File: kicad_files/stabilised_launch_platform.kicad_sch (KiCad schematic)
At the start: 2 parts

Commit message: Added further components to schematic
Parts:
- added C? (x3): 10u, symbol Device:C
- added C? (x4): 0.1u, symbol Device:C
- added C?: 1u, symbol Device:C
- added J? (x2): Conn_01x03_Male, symbol Connector:Conn_01x03_Male
- added J?: Conn_01x04_Male, symbol Connector:Conn_01x04_Male
- added R? (x2): R, symbol Device:R
- added RV? (x3): R_Potentiometer, symbol Device:R_Potentiometer
- added SW?: SW_Push, symbol Switch:SW_Push
- added U?: AP7370-33Y, Package_TO_SOT_SMD:SOT-89-3, symbol Regulator_Linear:AP7384-33Y
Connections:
- net SCL: now reaches U?.10 (PA4)
- net SCL: now also R?.2
- net POT1: now reaches U?.13 (PA7)
- net POT1: now also RV?.2
- net GND: now reaches U?.15 (VSS)
- net GND: now also U?.3 (GND), C?.2, C?.2, C?.2, C?.2, C?.2, C?.2, C?.2, C?.2, J?.3 (Pin_3), J?.3 (Pin_3), J?.4 (Pin_4), RV?.3, RV?.3, RV?.3, SW?.1, U?.2 (GND)
- net +3.3V: now reaches U?.16 (VDD)
- net +3.3V: now also U?.1 (V+), U?.5 (VDDA), C?.1, C?.1, C?.1, C?.1, C?.1, C?.1, R?.1, R?.1, RV?.1, RV?.1, RV?.1, U?.1 (VO)
- net SDA: now reaches U?.18 (PA10)
- net SDA: now also R?.2
- net SWDIO: now reaches U?.19 (PA13)
- net SWDIO: now also J?.2 (Pin_2)
- net SWCLK: now reaches U?.20 (PA14)
- net SWCLK: now also J?.3 (Pin_3)
- net at U?.4 (NRST): now also C?.1, SW?.2
- net HSE_OSC: now reaches U?.6 (PA0)
- net HSE_OSC: now also U?.2 (CLOCK)
- new net +5V: C?.1, J?.1 (Pin_1), J?.2 (Pin_2), J?.2 (Pin_2), U?.3 (VI)
- new net POT2: RV?.2
- new net POT3: RV?.2
- new net SERVO1_SIG: J?.1 (Pin_1)
- new net SERVO2_SIG: J?.1 (Pin_1)
- no-connect marks 0 -> 2
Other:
- note added: "8MHz External Clock"
- note added: "MCU Decoupling Capacitors"
- note added: "PID Gain Potentiometers"
- note added: "ST-LINK Connector"
- note added: "Servo Motor Connectors"
- note added: "Voltage Regulator"
- moved on the sheet: U?

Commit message: component values
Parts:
- R1, R2: renamed from R?; value R -> 2.2k
- gave numbers to parts that had none: 18

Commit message: added more components
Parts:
- removed J3: Conn_01x04_Male, symbol Connector:Conn_01x04_Male
- added C10, C13: 47p, symbol Device:C
- added C11: 10n, symbol Device:C
- added C12, C9: 0.1u, symbol Device:C
- added C14: 4.7u, symbol Device:C_Polarized
- added FB1: FerriteBead, symbol Device:FerriteBead
- added J3: Conn_01x06_Male, symbol Connector:Conn_01x06_Male
- added J4: USB_C_Receptacle_USB2.0, symbol Connector:USB_C_Receptacle_USB2.0
- added JP1: SolderJumper, symbol Jumper:SolderJumper_2_Open
- added R3, R4: 5.1k, symbol Device:R
- added R5, R6: 2.2k, symbol Device:R
- added U4: FT201XS, Package_SO:SSOP-16_3.9x4.9mm_P0.635mm, symbol Interface_USB:FT201XS
- R1, R2: value 2.2k -> 27R
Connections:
- net +3.3V: now also U3.1 (PB9), R5.1, R6.1; no longer R1.1, R2.1
- net +5V: now also C14.1, C9.1, FB1.2, J3.1 (Pin_1), JP1.1 (A)
- net GND: now also C10.2, C11.2, C12.2, C13.2, C14.2, C9.2, J3.6 (Pin_6), J4.A1 (GND), J4.A12 (GND), J4.B1 (GND), J4.B12 (GND), J4.S1 (SHIELD), R3.2, R4.2, U4.13 (GND), U4.5 (GND)
- net POT1: now also U3.11 (PA5); no longer U3.13 (PA7)
- net POT2: now also U3.12 (PA6)
- net POT3: now also U3.13 (PA7)
- net SCL: now also U3.17 (PA9), R5.2, U4.2 (SCL); no longer R1.2, U3.10 (PA4)
- net SDA: now also R6.2, U4.4 (SDA); no longer R2.2
- net SERVO1_SIG: now also U3.7 (PA1)
- net SERVO2_SIG: now also U3.10 (PA4)
- net SWCLK: now also J3.3 (Pin_3)
- net SWDIO: now also J3.2 (Pin_2)
- net MCU_TX: now reaches U3.8 (PA2)
- net MCU_TX: now also J3.4 (Pin_4)
- net MCU_RX: now reaches U3.9 (PA3)
- net MCU_RX: now also J3.5 (Pin_5)
- new net: J4.B5 (CC2), R4.1
- new net: R2.2, U4.8 (USBDP)
- new net: JP1.2 (B), U4.12 (VCC)
- new net: R1.2, U4.9 (USBDM)
- new net: J4.A5 (CC1), R3.1
- new net: C11.1, FB1.1, J4.A4 (VBUS), J4.A9 (VBUS), J4.B4 (VBUS), J4.B9 (VBUS)
- new net FTDI_3V3: C12.1, U4.10 (3V3OUT), U4.11 (~{RESET}), U4.3 (VCCIO)
- new net USBDM: C13.1, J4.A7 (D-), J4.B7 (D-), R1.1
- new net USBDP: C10.1, J4.A6 (D+), J4.B6 (D+), R2.1
- no-connect marks 2 -> 11
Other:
- note added: "I2C Pull-up"
- note added: "Microcontroller"
- note added: "USB C Receptacle"
- note added: "USB to I2C"
- moved on the sheet: RV1, RV2, RV3

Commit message: Schematic finished
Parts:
- added Q1, Q2: AO3400A, Package_TO_SOT_SMD:SOT-23, symbol Transistor_FET:AO3400A
- added R7, R8: 4.7k, Resistor_SMD:R_0805_2012Metric_Pad1.20x1.40mm_HandSolder, symbol Device:R
- added U5: LIS3DH, Package_LGA:LGA-16_3x3mm_P0.5mm_LayoutBorder3x5y, symbol Sensor_Motion:LIS3DH
- C1, C10, C11, C12, C13, C14, C2, C3, C4, C5, C6, C7, C8, C9: footprint (none) -> Capacitor_SMD:C_0805_2012Metric_Pad1.18x1.45mm_HandSolder
- J1, J2: footprint (none) -> Connector_PinHeader_1.00mm:PinHeader_1x03_P1.00mm_Vertical
- J3: footprint (none) -> Connector_PinHeader_1.00mm:PinHeader_1x06_P1.00mm_Vertical
- J4: footprint (none) -> Connector_USB:USB_C_Receptacle_GCT_USB4085
- R1, R2, R3, R4, R5, R6: footprint (none) -> Resistor_SMD:R_0805_2012Metric_Pad1.20x1.40mm_HandSolder
- RV1, RV2, RV3: footprint (none) -> Potentiometer_THT:Potentiometer_Bourns_PTA4543_Single_Slide
- SW1: footprint (none) -> Button_Switch_SMD:SW_SPST_PTS645
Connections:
- net +3.3V: now also U5.14 (VDD)
- net +5V: now also R7.1, R8.1
- net GND: now also Q1.2 (S), Q2.2 (S), U5.10 (GND), U5.12 (GND), U5.5 (GND)
- net SCL: now also U5.4 (SCL/SPC)
- net SDA: now also U5.6 (SDA/SDI/SDO)
- net SERVO1_SIG: now also Q1.1 (G)
- net SERVO2_SIG: now also Q2.1 (G)
- new net SERVO1_SIG_AMP: Q1.3 (D), R7.2
- new net SERVO2_SIG_AMP: Q2.3 (D), R8.2
- no-connect marks 11 -> 19
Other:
- note added: "Accelerometer"
- note added: "Servo Signal Amplification"
- moved on the sheet: C1, C2, C3, C4, C5, C6, C7, C8, J1, J2, J3, R5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

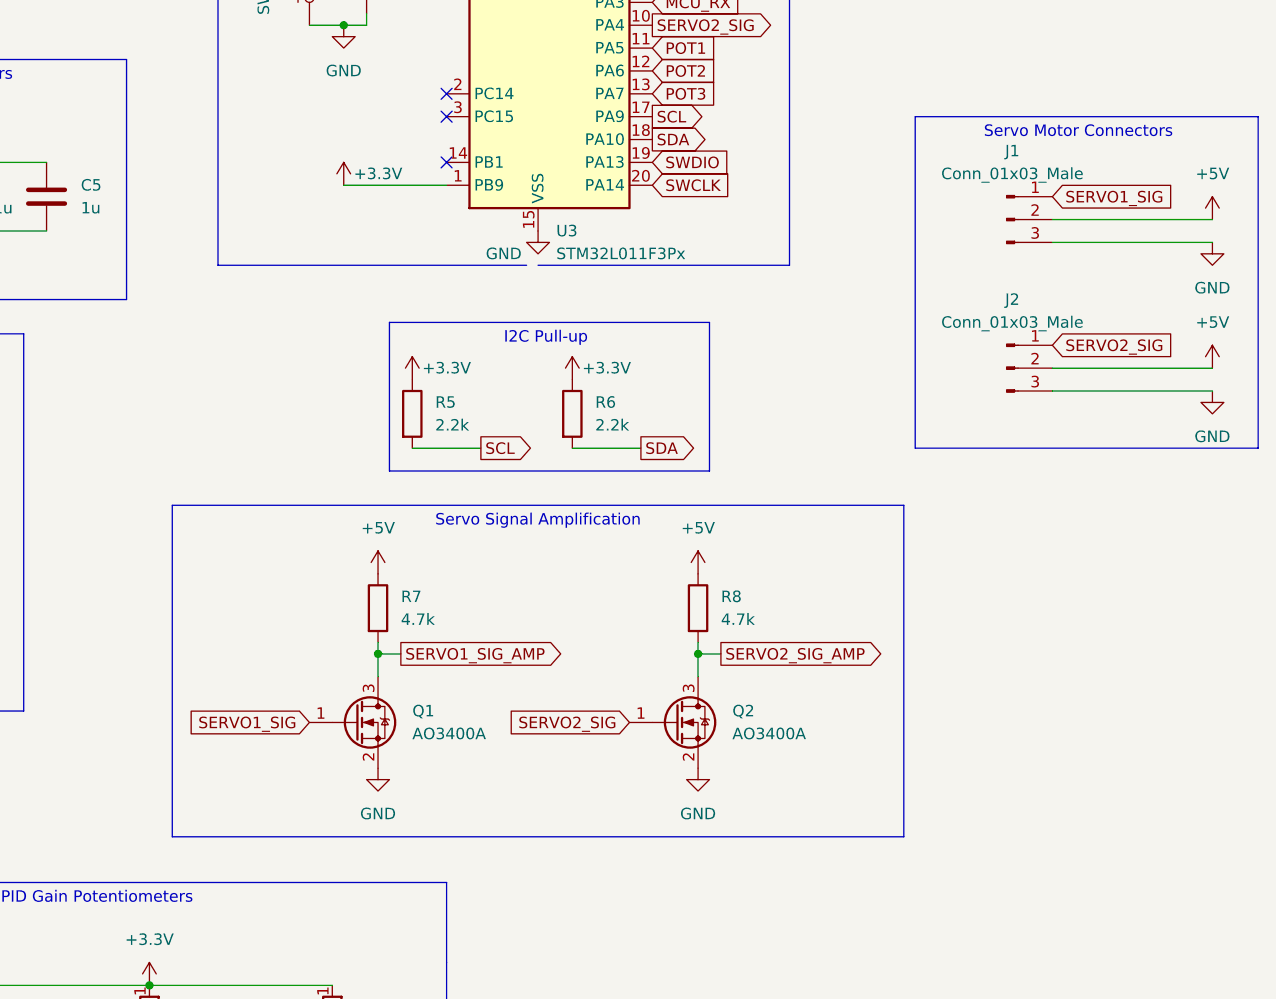
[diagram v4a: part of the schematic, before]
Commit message: Removed unnecessary mosfets, schematic finished
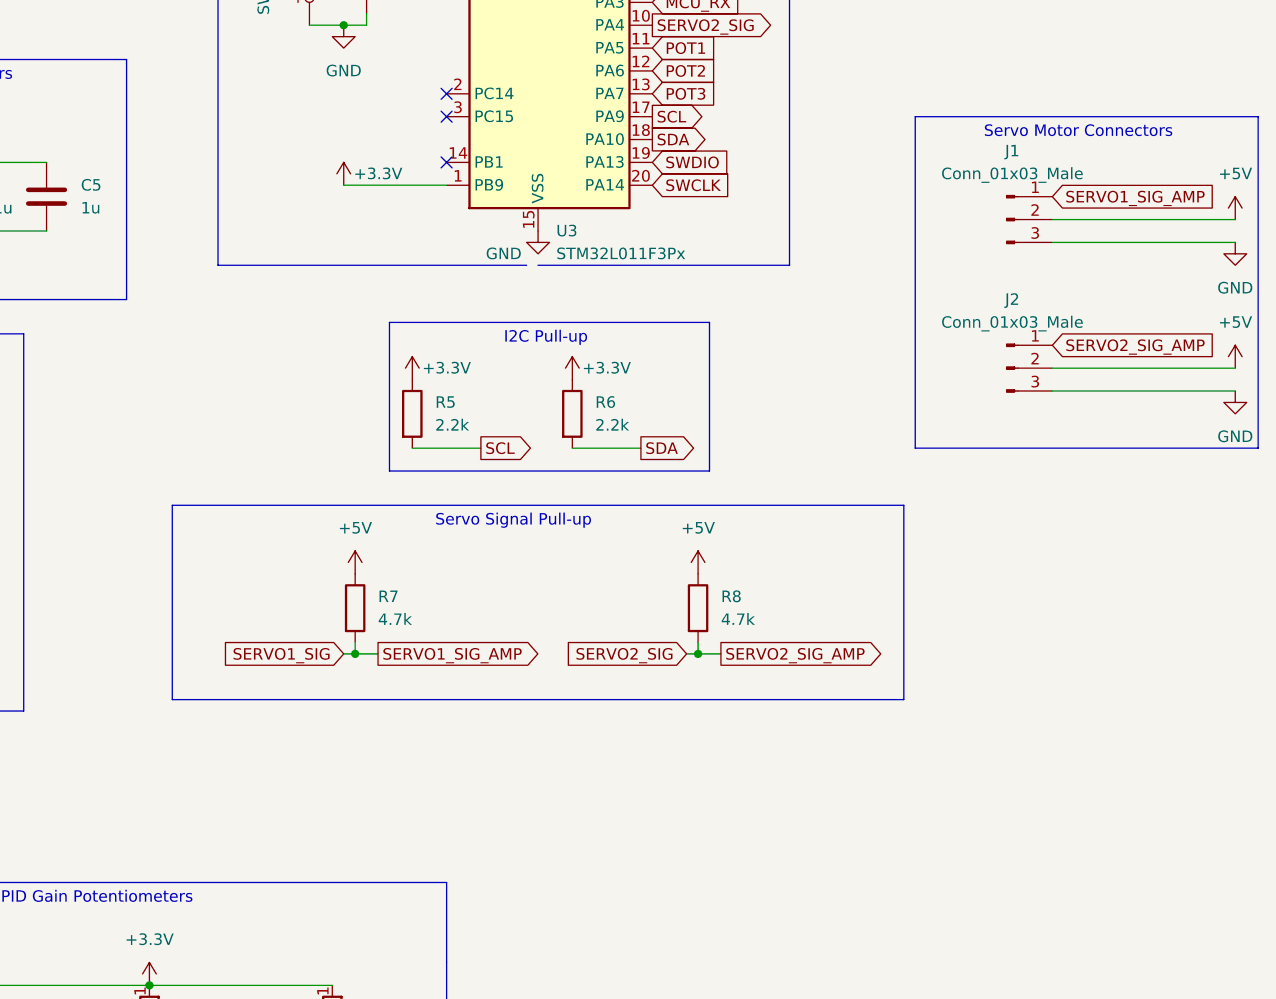
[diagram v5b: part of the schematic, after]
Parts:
- removed Q1, Q2: AO3400A, Package_TO_SOT_SMD:SOT-23, symbol Transistor_FET:AO3400A
- FB1: footprint (none) -> Inductor_SMD:L_0805_2012Metric_Pad1.05x1.20mm_HandSolder
- JP1: footprint (none) -> Jumper:SolderJumper-2_P1.3mm_Open_Pad1.0x1.5mm
- U5: footprint Package_LGA:LGA-16_3x3mm_P0.5mm_LayoutBorder3x5y -> CustomFootprints:LIS3DH Accelerometer
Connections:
- net SERVO1_SIG_AMP is gone; now on net SERVO1_SIG: R7.2
- net SERVO2_SIG_AMP is gone; now on net SERVO2_SIG: R8.2
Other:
- note added: "Servo Signal Pull-up"
- note removed: "Servo Signal Amplification"
- moved on the sheet: R7
